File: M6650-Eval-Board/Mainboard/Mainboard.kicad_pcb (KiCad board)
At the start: 2 copper layers, 92.7 x 82.6 mm, 65 parts, among them J1 MB, J10 Parallel, J11 Serial, J12 5V, J13 5V, J14 Misc, J15 Line Out, J16 AUD, J2 MR, J3 MT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

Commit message: I screwed up some jumper high/low states but not rerouting now so just silkscreen edit
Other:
- board text added: "SERIAL !STBY !RND PORTL"
- board text removed: "SERIAL STBY RND PORTL"
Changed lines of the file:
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@@
     (effects (font (size 1.25 0.83) (thickness 0.15)) (justify left))
   )
-  (gr_text "SERIAL\nSTBY\nRND\nPORTL" (at 57.15 62.23 90) (layer "F.SilkS")
+  (gr_text "SERIAL\n!STBY\n!RND\nPORTL" (at 57.15 62.23 90) (layer "F.SilkS")
     (effects (font (size 1 1) (thickness 0.15)) (justify right top))
   )

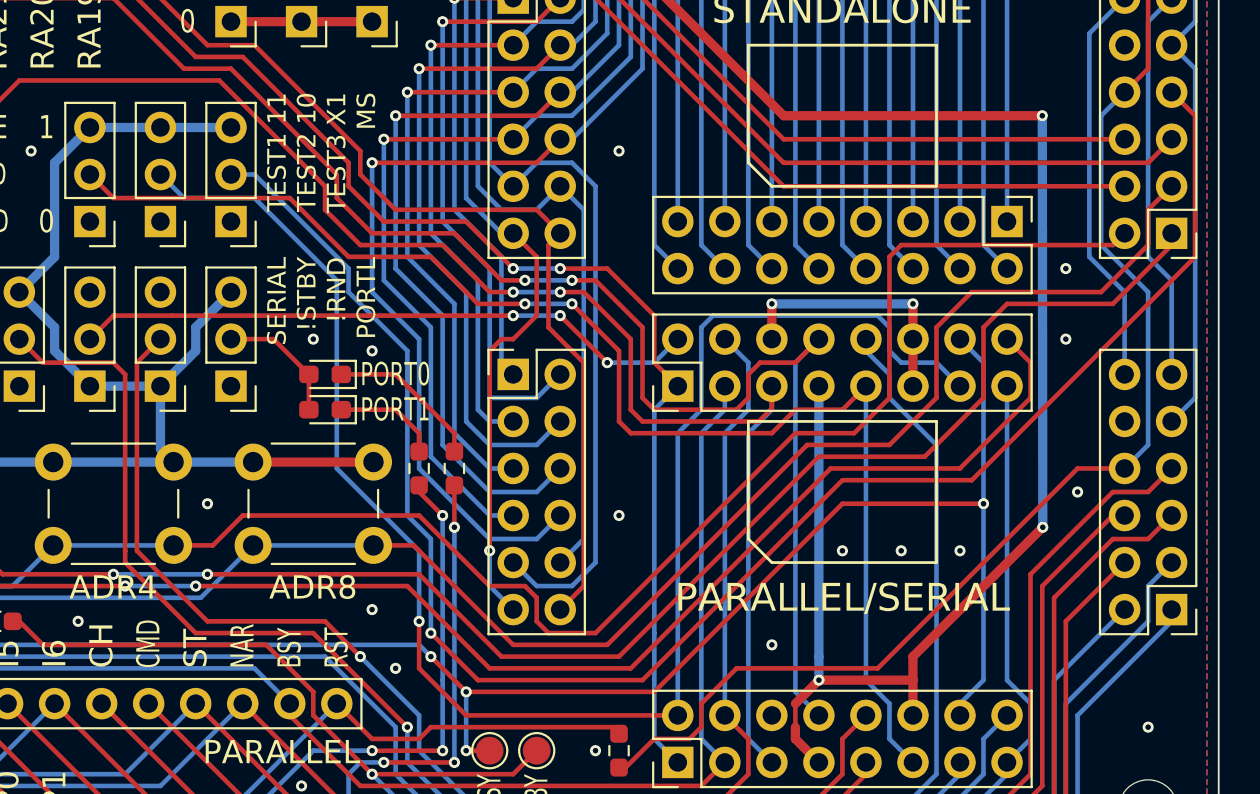
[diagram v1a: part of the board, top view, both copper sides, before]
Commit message: Fix XTCR pin for standalone mode
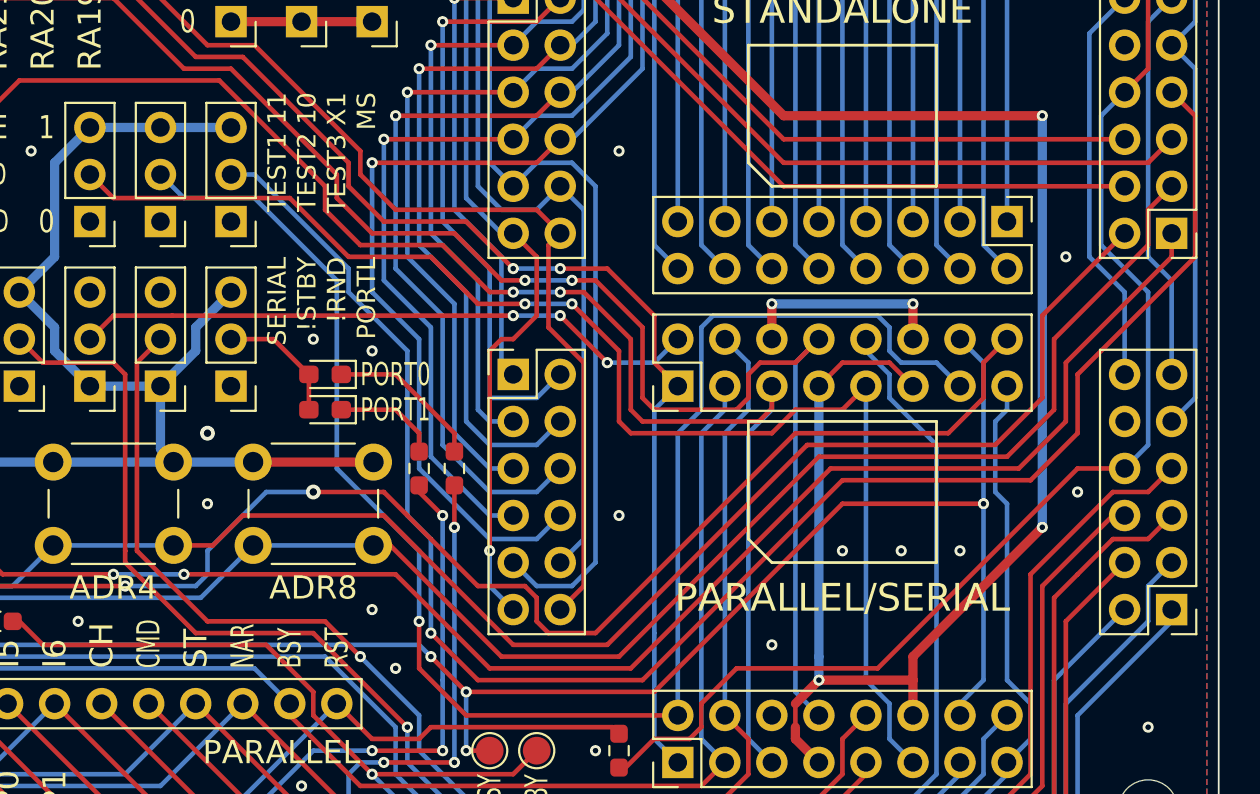
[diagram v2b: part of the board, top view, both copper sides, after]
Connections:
- J5 pad 11: /GND -> /5V
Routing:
- net /5V: track 447.7 -> 453.8 mm
- net /GND: track 47.5 -> 45.0 mm
- net /SW2: track 104.6 -> 102.5 mm
- net /TEST3: track 91.2 -> 93.1 mm
- net /SW0: track 93.8 -> 95.4 mm
- net /SW3: track 106.6 -> 107.1 mm
- net /SW1: track 103.7 -> 104.3 mm
- net /STANDBY: track 91.9 -> 92.4 mm

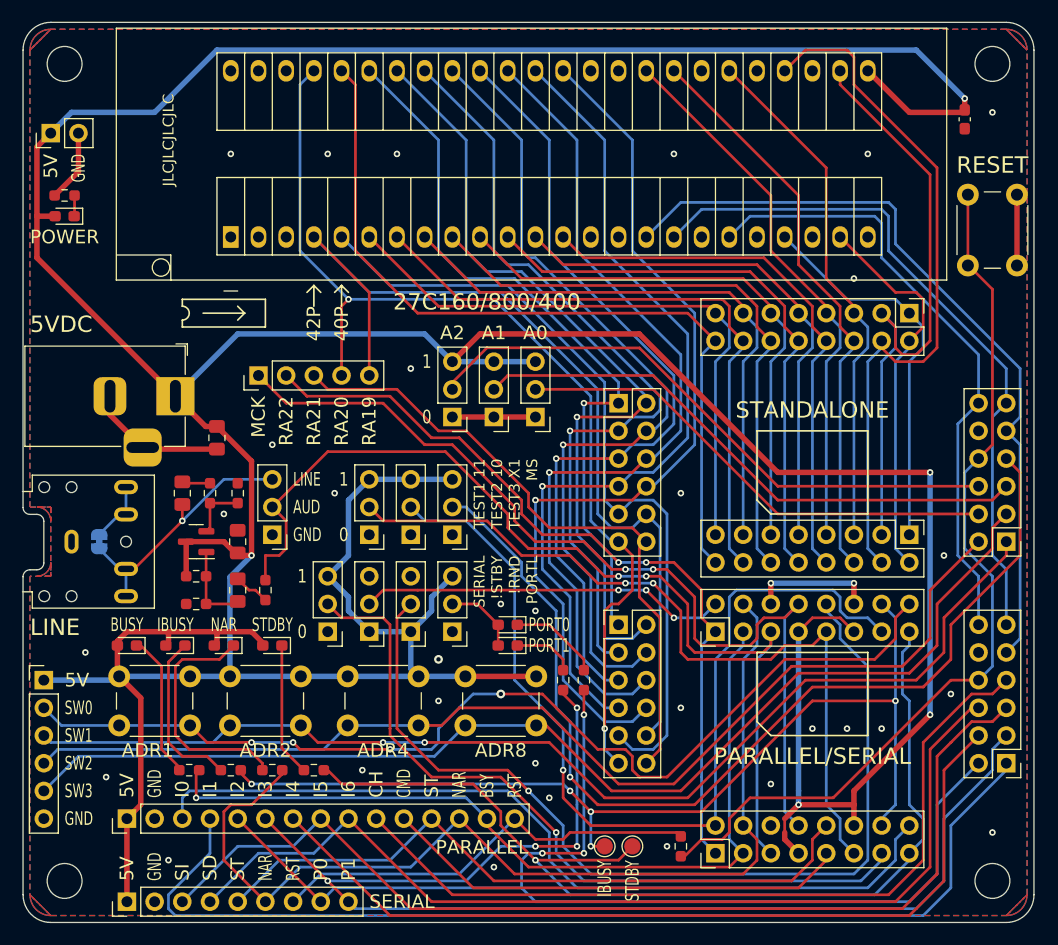
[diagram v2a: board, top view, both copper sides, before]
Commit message: Add debounce to manual parallel board, redo board edges and clearance rules
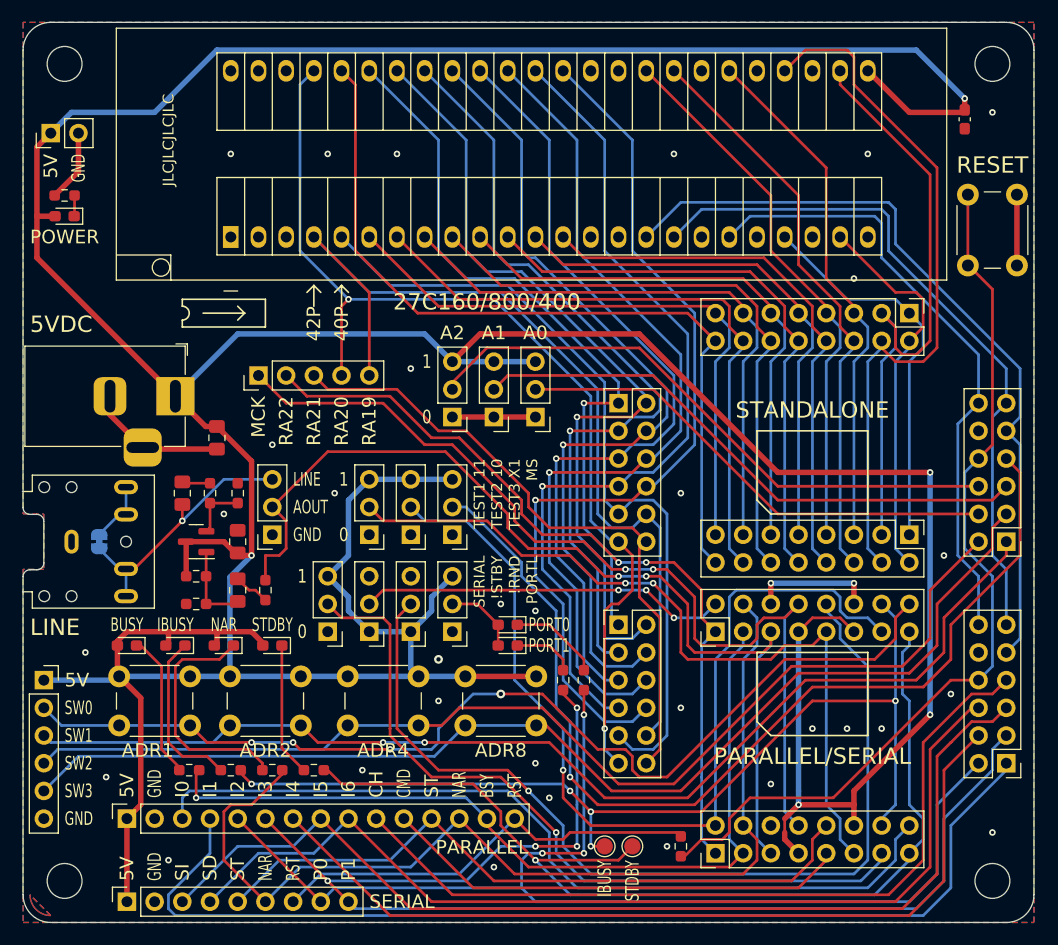
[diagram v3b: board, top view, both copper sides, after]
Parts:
- C3: value 10u -> 1u
- J10: footprint Connector_PinHeader_2.54mm:PinHeader_1x15_P2.54mm_Vertical -> Connector_PinSocket_2.54mm:PinSocket_1x15_P2.54mm_Vertical
- J11: footprint Connector_PinHeader_2.54mm:PinHeader_1x09_P2.54mm_Vertical -> Connector_PinSocket_2.54mm:PinSocket_1x09_P2.54mm_Vertical
- J16: footprint Connector_PinHeader_2.54mm:PinHeader_1x03_P2.54mm_Vertical -> Connector_PinSocket_2.54mm:PinSocket_1x03_P2.54mm_Vertical
- J9: footprint Connector_PinHeader_2.54mm:PinHeader_1x06_P2.54mm_Vertical -> Connector_PinSocket_2.54mm:PinSocket_1x06_P2.54mm_Vertical
- R10, R9: value 1K -> 100K
- R8: value 2K2 -> 100K
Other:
- board text added: "AOUT"
- board text removed: "AUD"
